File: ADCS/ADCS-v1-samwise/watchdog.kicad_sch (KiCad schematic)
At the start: 28 parts, among them U7 TLV1704

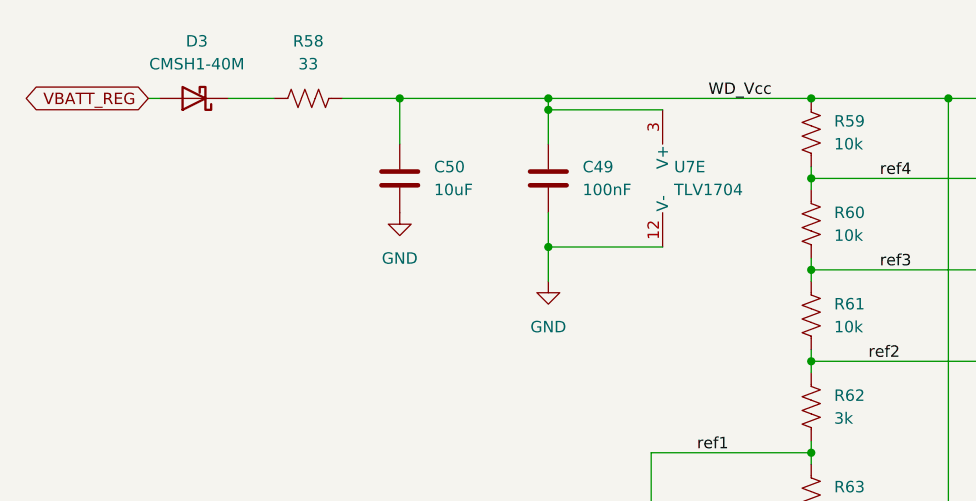
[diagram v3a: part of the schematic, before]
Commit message: Add watchdog 6v regulator
To schematic, still needs added on pcb. Schematic needs to be checked idk what I'm doing lol
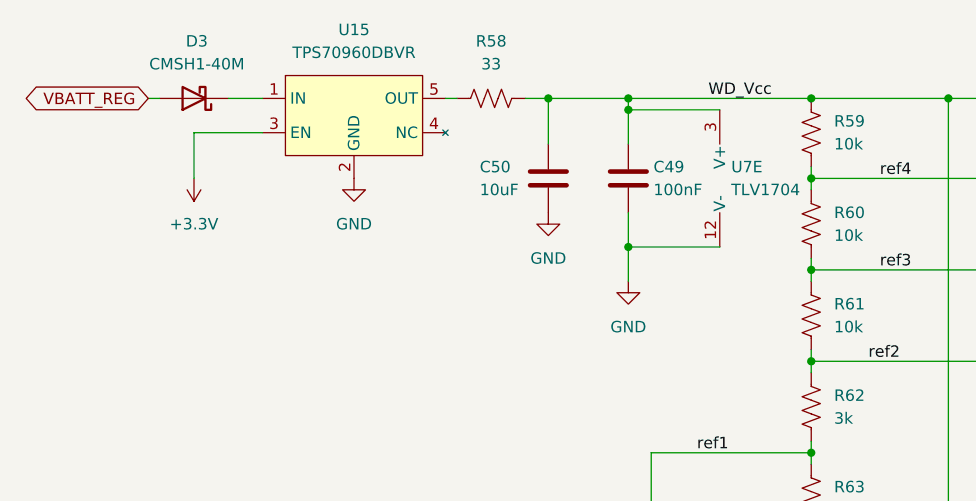
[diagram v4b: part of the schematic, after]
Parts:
- added U15: TPS70960DBVR, Package_TO_SOT_SMD:SOT-23-5, symbol ssi_IC:TPS70960DBVR
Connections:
- net GND: now also U15.2 (GND)
- net at R58.1: now also U15.5 (OUT); no longer D3.1 (K)
- new net: D3.1 (K), U15.1 (IN)
- new net +3.3V: U15.3 (EN)
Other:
- moved on the sheet: C49, C50, R58, U7E

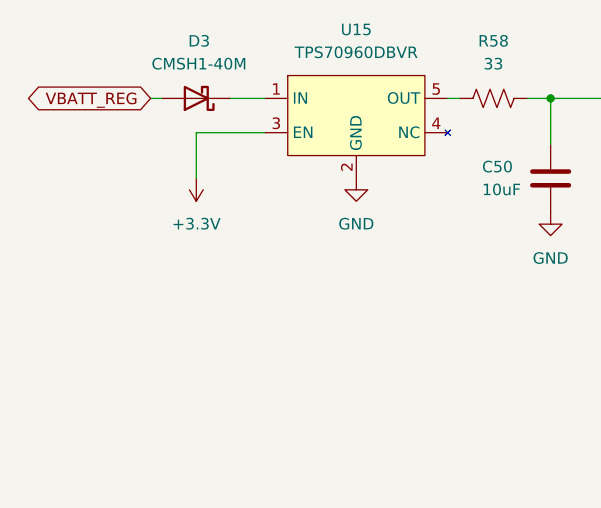
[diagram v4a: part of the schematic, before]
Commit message: Add watchdog regulator
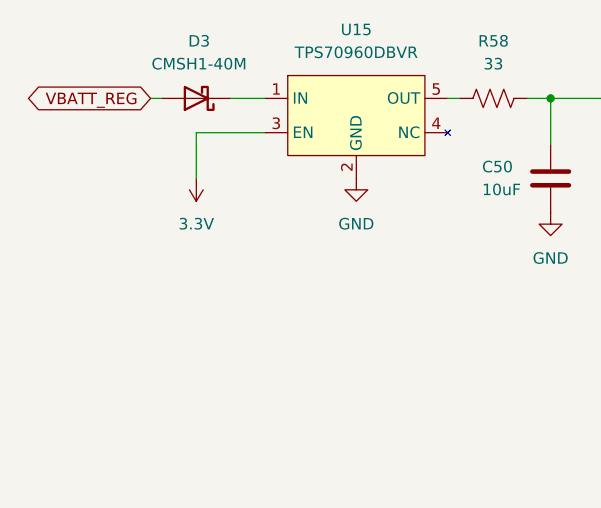
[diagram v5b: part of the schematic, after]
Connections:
- net +3.3V renamed 3.3V
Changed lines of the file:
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@@
+	)
+	(symbol
+		(lib_id "power:+3V3")
+		(at 30.48 50.8 180)
+		(unit 1)
+		(exclude_from_sim no)
+		(in_bom yes)
+		(on_board yes)
+		(dnp no)
+		(fields_autoplaced yes)
+		(property "Reference" "#PWR015"
+			(at 30.48 46.99 0)
+			(effects
+				(font
+					(size 1.27 1.27)
+				)
+				(hide yes)
+			)
+		)
+		(property "Value" "3.3V"
+			(at 30.48 55.88 0)
+			(effects
+				(font
+					(size 1.27 1.27)
+				)
+			)
+		)
+		(property "Footprint" ""
+			(at 30.48 50.8 0)
+			(effects
+				(font
+					(size 1.27 1.27)
+				)
+				(hide yes)
+			)
+		)
+		(property "Datasheet" ""
+			(at 30.48 50.8 0)
+			(effects
+				(font
+					(size 1.27 1.27)
+				)
+				(hide yes)
+			)
+		)
+		(property "Description" "Power symbol creates a global label with name \"+3V3\""
+			(at 30.48 50.8 0)
+			(effects
+				(font
+					(size 1.27 1.27)
+				)
+				(hide yes)
+			)
+		)
+		(pin "1"
+		)
+		(instances
+			(project "ADCS_board"
+				(path "/db20b18b-d25a-428e-8229-70a189e1de75/a393ea4a-5f4e-4c0f-917f-6d28e91dd546"
+					(reference "#PWR015")
+					(unit 1)
+				)
+			)
+		)
 	)
 	(symbol
@@
 					(unit 1)
 				)
-			)
-		)
-	)
-	(symbol
-		(lib_id "power:+3.3V")
-		(at 30.48 50.8 180)
-		(unit 1)
-		(exclude_from_sim no)
-		(in_bom yes)
-		(on_board yes)
-		(dnp no)
-		(fields_autoplaced yes)
-		(property "Reference" "#PWR015"
-			(at 30.48 46.99 0)
-			(effects
-				(font
-					(size 1.27 1.27)
-				)
-				(hide yes)
-			)
-		)
-		(property "Value" "+3.3V"
-			(at 30.48 55.88 0)
-			(effects
-				(font
-					(size 1.27 1.27)
-				)
-			)
-		)
-		(property "Footprint" ""
-			(at 30.48 50.8 0)
-			(effects
-				(font
-					(size 1.27 1.27)
-				)
-				(hide yes)
-			)
-		)
-		(property "Datasheet" ""
-			(at 30.48 50.8 0)
-			(effects
-				(font
-					(size 1.27 1.27)
-				)
-				(hide yes)
-			)
-		)
-		(property "Description" "Power symbol creates a global label with name \"+3.3V\""
-			(at 30.48 50.8 0)
-			(effects
-				(font
-					(size 1.27 1.27)
-				)
-				(hide yes)
-			)
-		)
-		(pin "1"
-		)
-		(instances
-			(project ""
-				(path "/db20b18b-d25a-428e-8229-70a189e1de75/a393ea4a-5f4e-4c0f-917f-6d28e91dd546"
-					(reference "#PWR015")
-					(unit 1)
-				)
